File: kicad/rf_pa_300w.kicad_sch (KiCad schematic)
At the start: 21 parts, among them J1 Vdd 72.5V, J2 SMA 50ohm, J3 VCC 12V, J4 PWM IN, Q1 IRF540, Q2 IRF540, U1 IR2181S

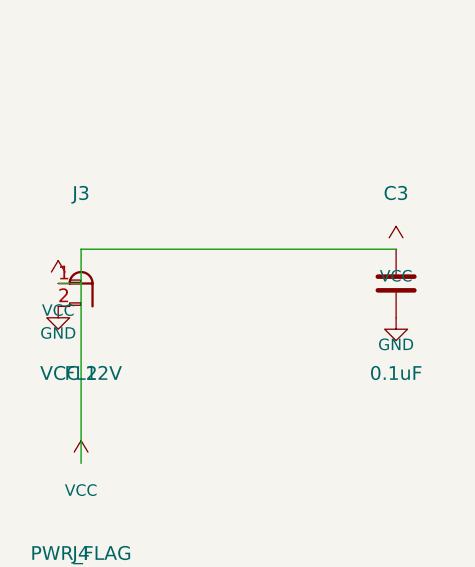
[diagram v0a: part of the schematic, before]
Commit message: Complete schematic wiring, PCB trace routing, DRC/ERC validation, and Gerber generation
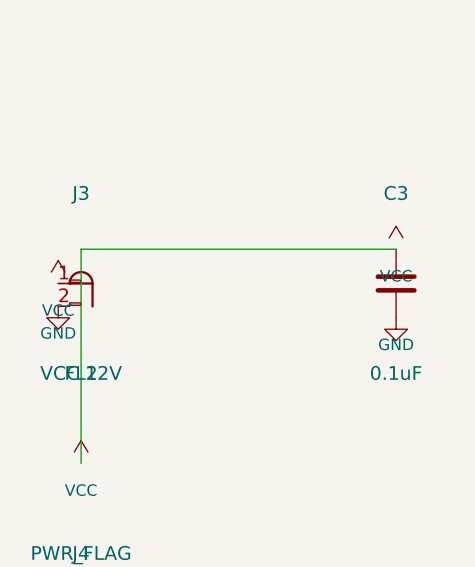
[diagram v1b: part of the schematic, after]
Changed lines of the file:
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@@
-	(wire
-		(pts
-			(xy 27.46 95) (xy 30 95)
-		)
-		(stroke
-			(width 0)
-			(type solid)
-		)
-	)
 	(wire
 		(pts
